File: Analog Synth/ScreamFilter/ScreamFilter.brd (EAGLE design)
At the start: 160 x 100 mm, 39 parts, among them IC1 TL084D, IC2 TL082D, Q1 J310, Q2 J310, Q3 J310, Q5 J310

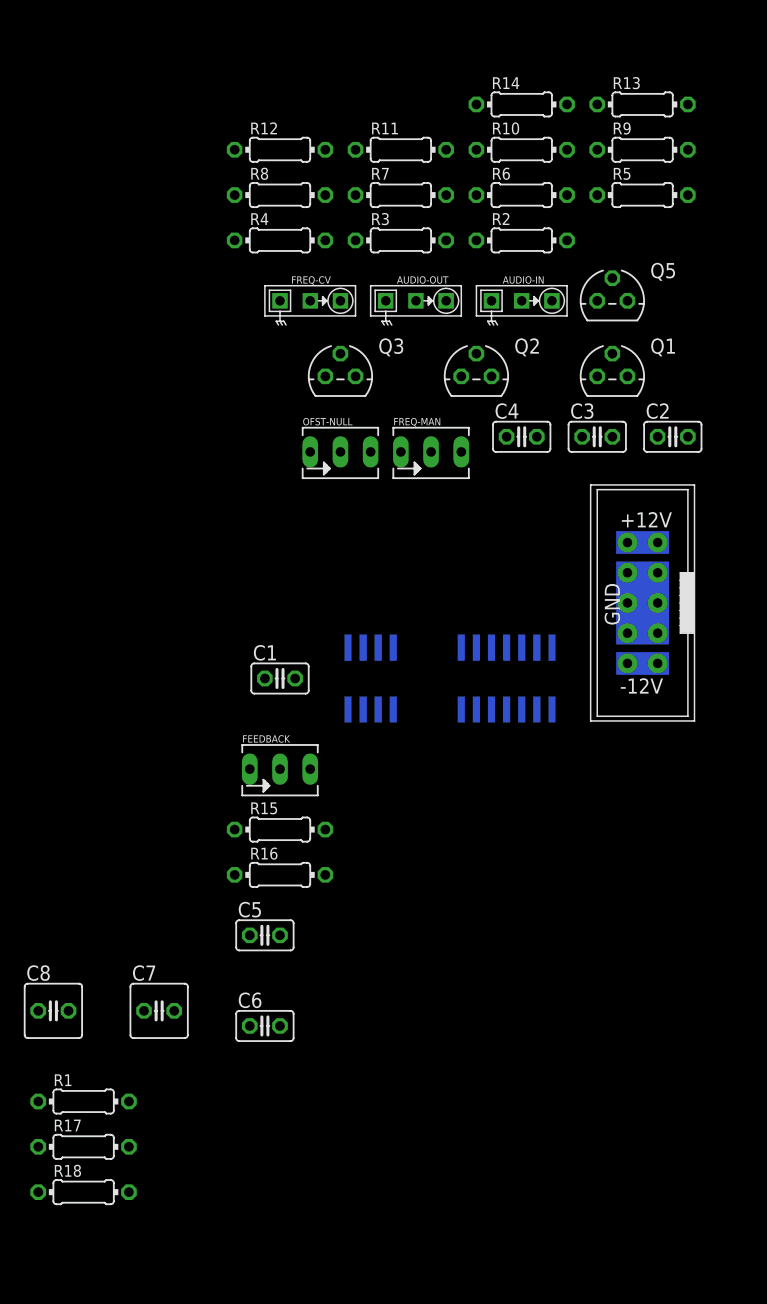
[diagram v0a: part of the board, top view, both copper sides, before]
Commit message: ScreamFilter v1.0; TODO: Add LEDs to ScreamFilter...   updated VCA-v2 for some reason.
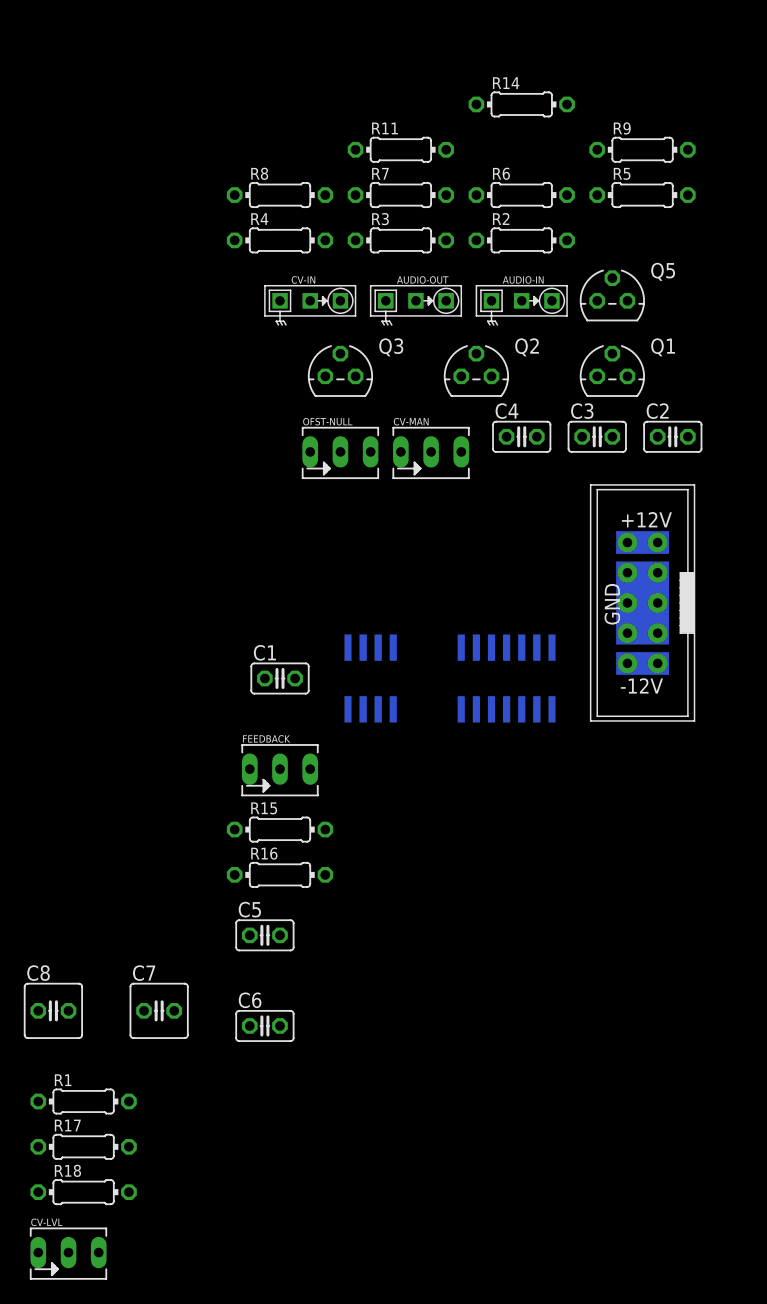
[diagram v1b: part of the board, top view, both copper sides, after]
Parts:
- removed R10: 180k, rcl:0204/7
- removed R12, R13: 100k, rcl:0204/7
- added CV-LVL: 100k LOG, pot:B64Y
- CV-MAN: value 100k LIN -> 10k LIN
- R1: value 180k -> 82k
- R11: value 2.2K -> 2.2k
- R17: value 33K -> 220k
- R18: value 12k -> 47k
- R7, R8: value 33K -> 100k
- R9: value 180k -> 47k
- renumbered FREQ-CV to CV-IN, FREQ-MAN to CV-MAN
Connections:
- removed net N$11: Q2.D
- removed net N$15: Q3.D
- removed net N$3: Q1.G, Q2.G, Q3.G, Q5.G, R1.2, R17.2, R18.2
- removed net N$7: Q5.D
- net +12V: no longer R7.2
- net GND: now also CV-LVL.A, R7.2; no longer R13.2
- net N$13: now also Q3.D
- net N$21: now also CV-LVL.E; no longer R9.1
- net N$22: no longer R10.2
- net N$23: now also Q1.G, Q2.G, Q3.G, Q5.G, R1.2, R17.2, R18.2; no longer R10.1
- net N$25: now also CV-LVL.S, R9.1; no longer IC2.6, R12.1, R13.1
- net N$30: now also IC2.6; no longer R12.2
- net N$6: now also Q5.D
- net N$9: now also Q2.D

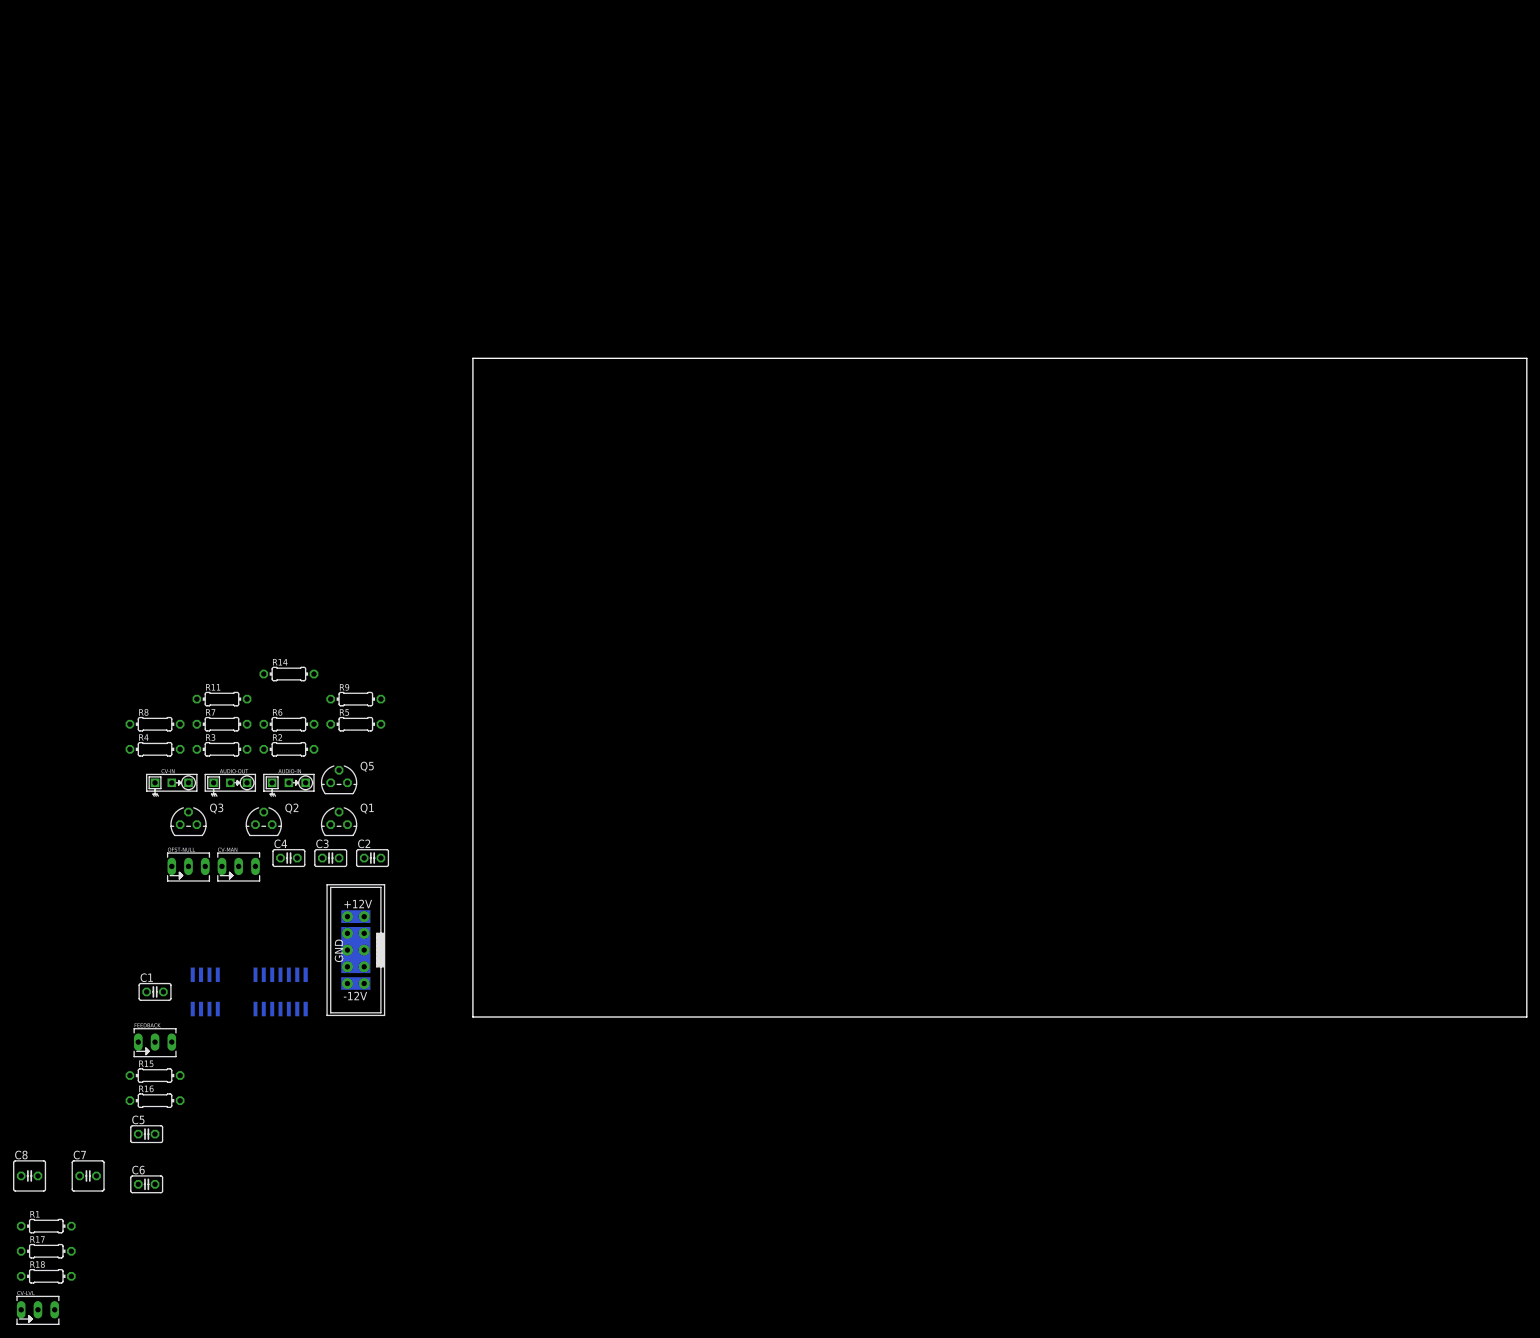
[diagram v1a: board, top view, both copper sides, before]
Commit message: VCA-v2 new schematic pdf; ScreamFilter layout has begun.
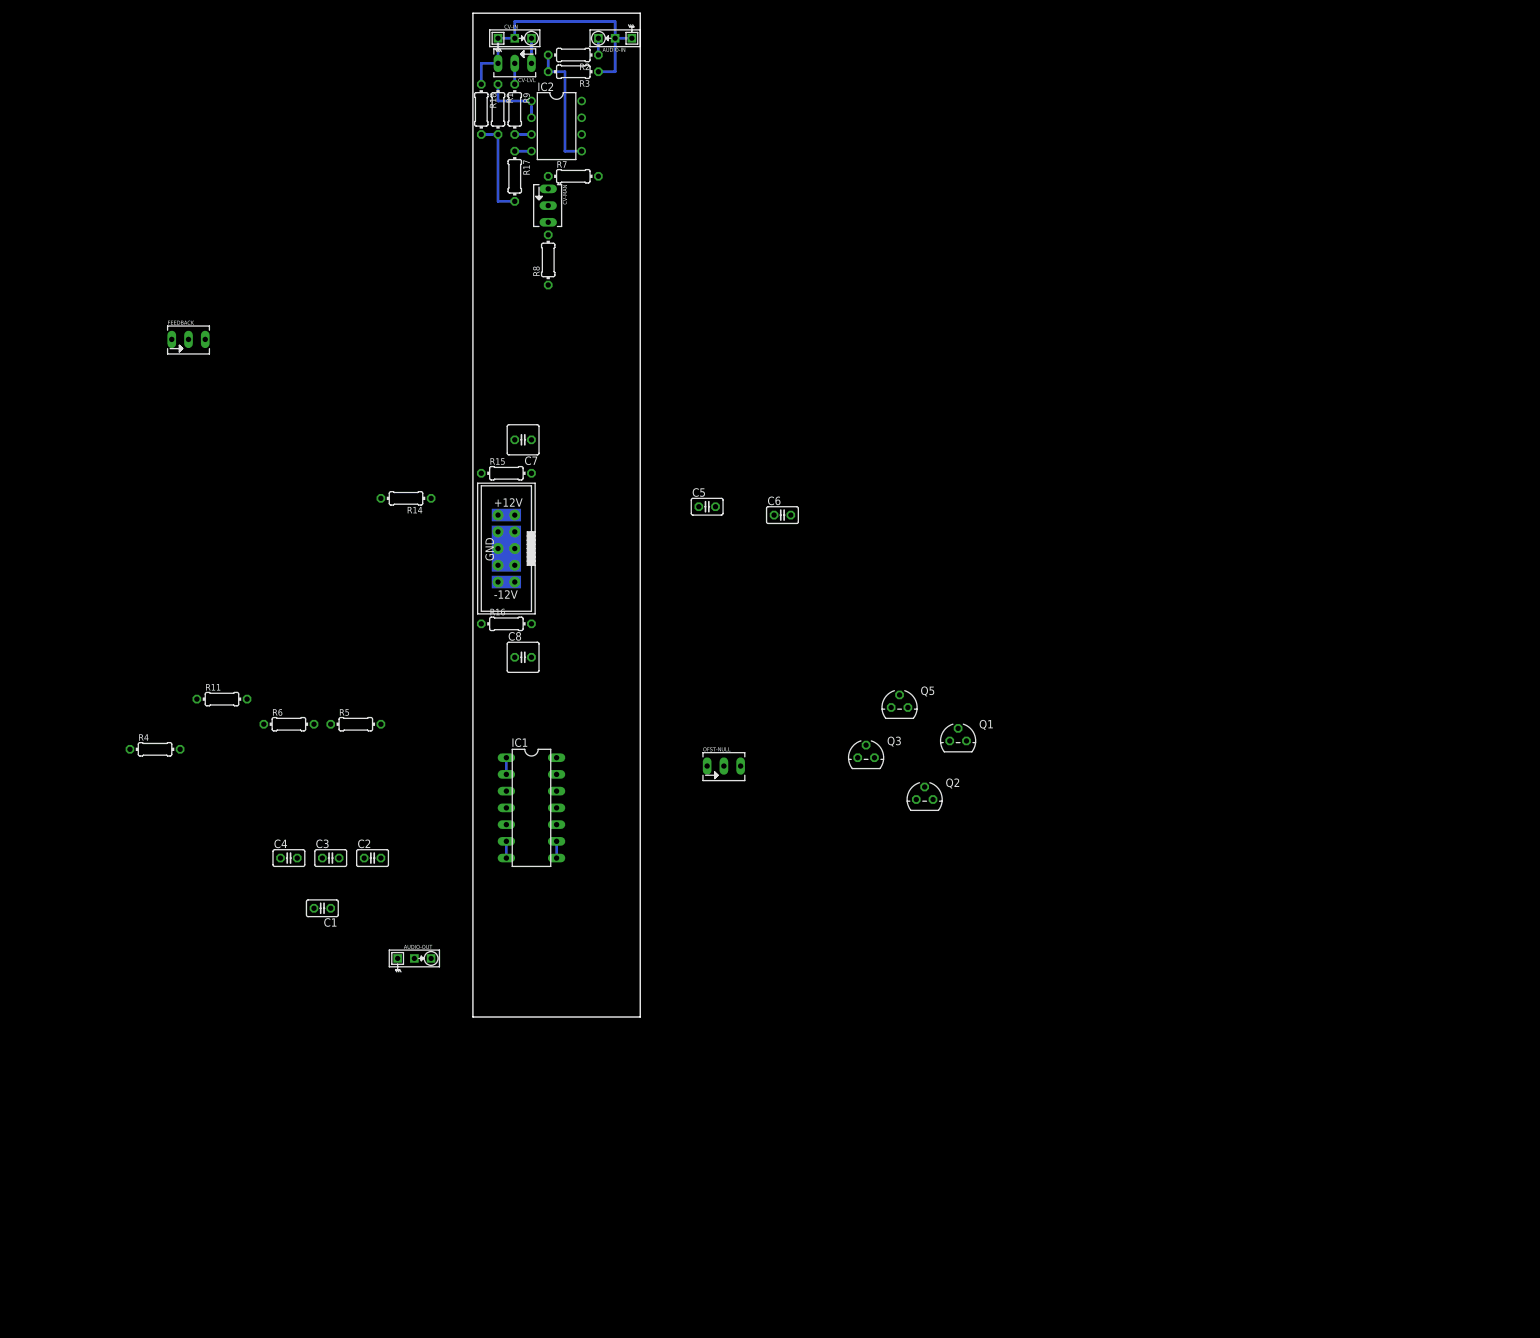
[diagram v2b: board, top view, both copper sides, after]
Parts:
- C7, C8: value (none) -> 100µ
- IC1: value TL084D -> TL084P; device linear:SO14 -> linear:DIL14
- IC2: value TL082D -> TL082P; device linear:SO08 -> linear:DIL08
- R15, R16: value 4.7 -> 7.5
- moved CV-LVL 202.6 mm to (6.35, 144.8), turned to 180 degrees
- moved R18 189.1 mm to (1.27, 137.8), turned to 270 degrees
- moved R1 182.9 mm to (3.81, 137.8), turned to 270 degrees
- moved R17 178.0 mm to (6.35, 127.6), turned to 270 degrees
- moved IC2 141.9 mm to (12.7, 135.3), flipped to the top, turned to 270 degrees
- moved C6 140.1 mm to (47.0, 76.2)
- moved C7 129.8 mm to (7.62, 87.6), turned to 180 degrees
- moved C5 127.7 mm to (35.6, 77.5)
- moved CV-IN 124.4 mm to (6.35, 148.6)
- moved AUDIO-IN 123.4 mm to (21.6, 148.6), turned to 180 degrees
- moved R3 115.9 mm to (15.2, 143.5), turned to 180 degrees
- moved R2 113.9 mm to (15.2, 146.1), turned to 180 degrees
- moved CV-MAN 110.8 mm to (11.4, 123.2), turned to 270 degrees
- moved C8 108.7 mm to (7.62, 54.6)
- moved FEEDBACK 106.8 mm to (-43.2, 102.9)
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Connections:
- net N$2: now also IC2.5; no longer IC2.3
- net N$22: now also IC2.3; no longer IC2.5
- net N$27: now also IC2.6; no longer IC2.2
- net N$30: now also IC2.1, IC2.2; no longer IC2.6, IC2.7
- net N$4: now also IC2.7; no longer IC2.1
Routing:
- net GND: track 0.00 -> 42.5 mm
- net N$2: track 0.00 -> 19.7 mm
- net N$23: track 0.00 -> 15.2 mm
- net N$30: track 0.00 -> 10.2 mm
- net N$21: track 0.00 -> 3.81 mm
- net N$25: track 0.00 -> 3.18 mm
- net N$9: track 0.00 -> 2.54 mm
- net N$13: track 0.00 -> 2.54 mm
- net N$22: track 0.00 -> 2.54 mm
- net -12V: track 0.00 -> 2.54 mm
- net N$6: track 0.00 -> 2.54 mm
- net N$1: track 0.00 -> 2.54 mm
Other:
- board size 160 x 100 mm -> 25.4 x 152.4 mm

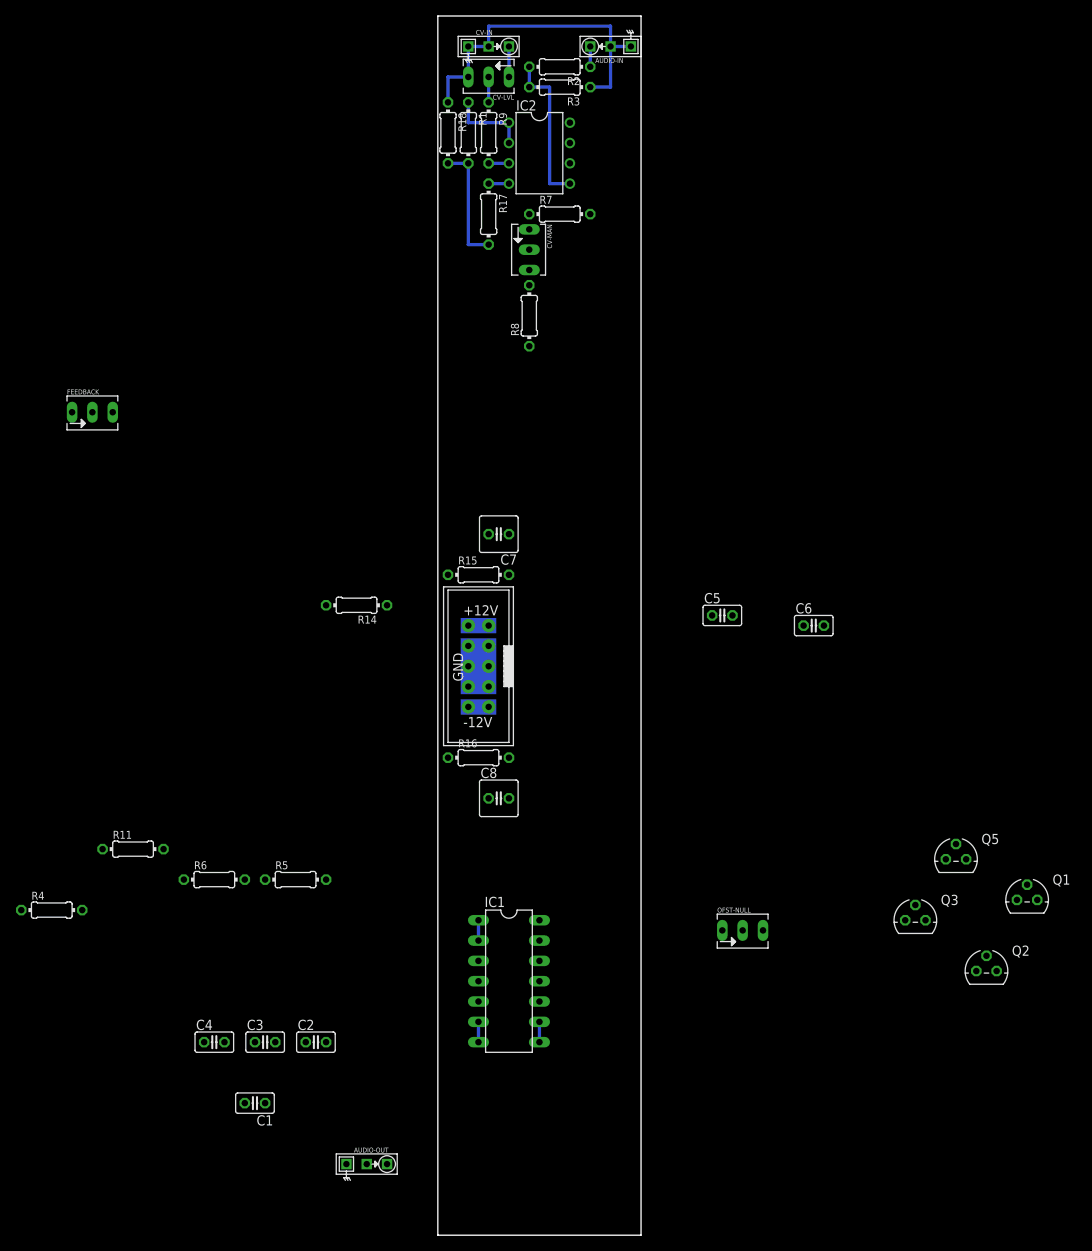
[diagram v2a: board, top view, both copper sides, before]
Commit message: working on ScreamFilter layout. close to finished
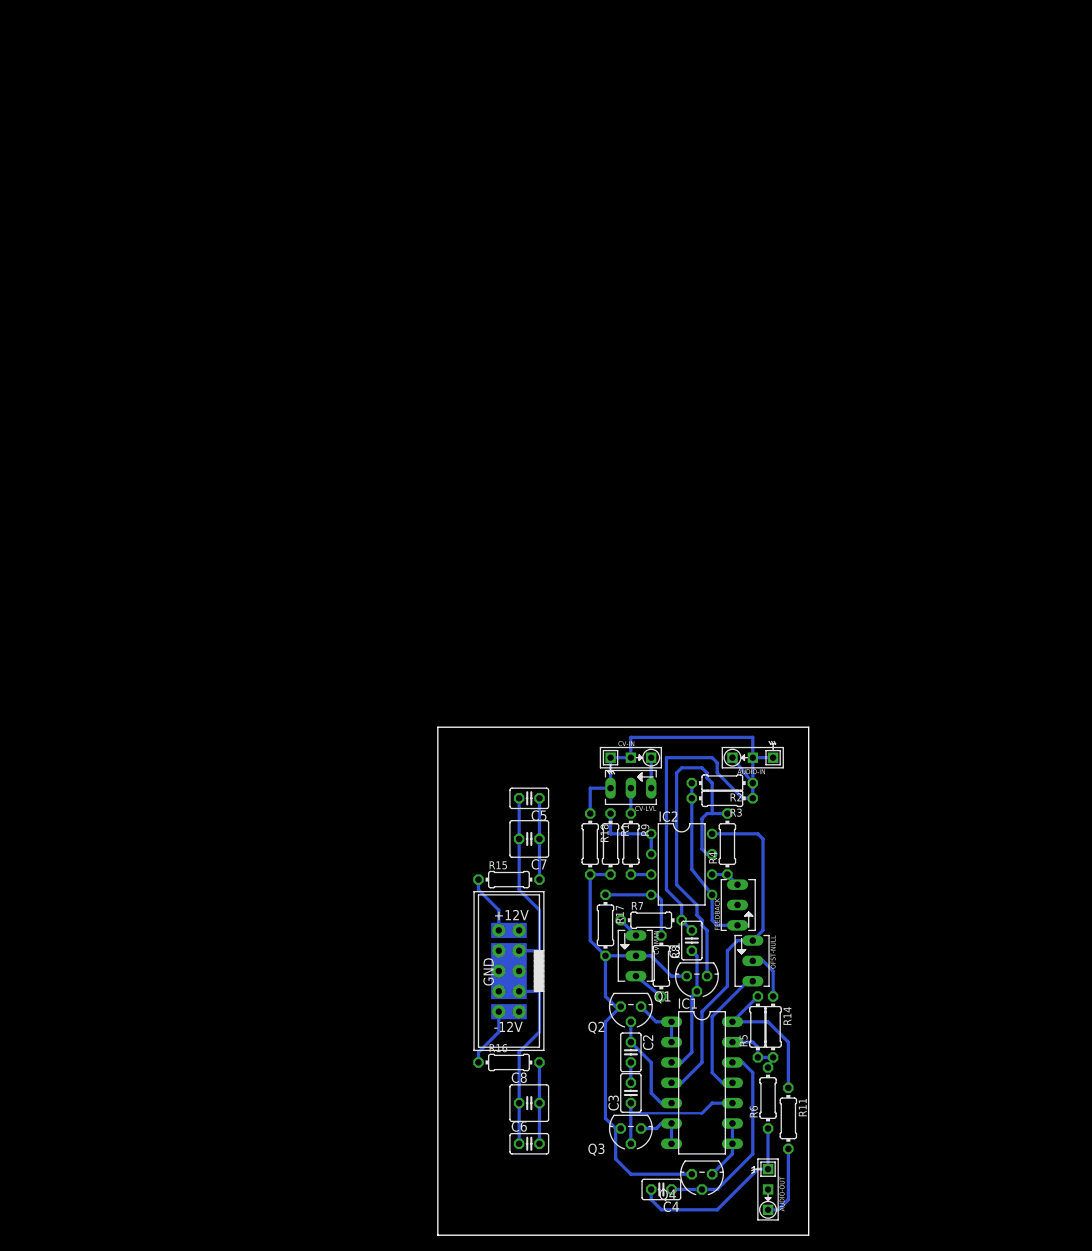
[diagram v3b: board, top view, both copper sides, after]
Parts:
- removed Q5: J310, transistor-small-signal:TO92R
- added Q4: J310, transistor-small-signal:TO92R
- moved FEEDBACK 101.5 mm to (37.5, 41.3), turned to 90 degrees
- moved R2 91.8 mm to (35.6, 56.5)
- moved R3 91.2 mm to (35.6, 54.6)
- moved AUDIO-IN 90.7 mm to (39.4, 59.7)
- moved CV-IN 90.7 mm to (24.1, 59.7)
- moved CV-LVL 90.7 mm to (24.1, 55.9)
- moved IC2 90.7 mm to (30.5, 46.4)
- moved R1 90.7 mm to (21.6, 48.9)
- moved R18 90.7 mm to (19.1, 48.9)
- moved R9 90.7 mm to (24.1, 48.9)
- moved R17 90.1 mm to (21.0, 38.7)
- moved CV-MAN 89.3 mm to (24.8, 34.9)
- moved R7 89.0 mm to (26.7, 39.4)
- moved R11 88.6 mm to (43.8, 14.6), turned to 270 degrees
- moved R4 84.9 mm to (36.2, 48.9), turned to 90 degrees
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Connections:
- net N$12: now also Q3.S; no longer Q2.S
- net N$13: now also Q4.D; no longer Q3.D
- net N$16: now also Q4.S; no longer Q3.S
- net N$23: now also Q4.G; no longer Q5.G
- net N$6: now also Q2.D; no longer Q5.D
- net N$8: now also Q2.S; no longer Q5.S
- net N$9: now also Q3.D; no longer Q2.D
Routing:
- net GND: track 42.5 -> 148.0 mm
- net +12V: track 0.00 -> 53.8 mm
- net N$23: track 15.2 -> 63.5 mm
- net N$4: track 0.00 -> 45.4 mm
- net -12V: track 2.54 -> 38.8 mm
- net N$16: track 0.00 -> 25.2 mm
- net N$12: track 0.00 -> 18.3 mm
- net N$10: track 0.00 -> 18.2 mm
- net N$5: track 0.00 -> 16.3 mm
- net N$8: track 0.00 -> 13.0 mm
- net N$24: track 0.00 -> 9.42 mm
- net N$19: track 0.00 -> 8.03 mm
- net N$29: track 0.00 -> 7.40 mm
- net N$28: track 0.00 -> 7.40 mm
- net N$18: track 0.00 -> 6.24 mm
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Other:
- board size 25.4 x 152.4 mm -> 46.4 x 63.5 mm
